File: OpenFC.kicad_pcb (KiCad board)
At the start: 8 copper layers, 29.5 x 27.6 mm, 173 parts, among them J1 5V, J13 5V, J14 5V, J15 5V, J16 5V, J17 5V, J18 5V, J19 5V, J2 5V, J20 5V, J21 5V, J22 5V, J23 5V, J24 5V, J25 5V, J26 5V, J27 5V, J28 5V, J29 5V, J3 5V, J30 5V, J31 5V, J32 5V, J33 5V, J34 5V, J35 5V, J36 5V, J37 5V, J38 5V, J39 5V, J4 5V, J40 5V, J41 5V, J42 5V, J43 5V, J44 5V, J45 5V, J46 5V, J47 5V, J48 5V, J5 5V, J53 5V, J57 5V, J59 5V, J6 5V, J7 5V, J8 5V, J9 5V, P1 SM08B-SRSS-TB(LF)(SN), Q7 DMN1150UFB-7B, U1 SM06B-SRSS-TB(LF)(SN), U10 TLV75533PDBVR, U11 RP2350A_C42411118, U12 ABM8-272-T3_C20625731, U13 W25Q32RVXHJQ TR, U14 LSM6DSV16XTR, U15 XL-1010RGBC-WS2812B, U16 XL-1010RGBC-WS2812B, U17 XL-1010RGBC-WS2812B, U18 XL-1010RGBC-WS2812B, U19 ESP8285H16, U2 W25Q128JVPIQTR, U20 SX1281IMLTRT, U21 TS2306A 240GF MSM 9_C2976675, U22 XL-1010RGBC-WS2812B, U23 XL-1010RGBC-WS2812B, U24 XL-1010RGBC-WS2812B, U25 XL-1010RGBC-WS2812B, U26 XL-1010RGBC-WS2812B, U27 XL-1010RGBC-WS2812B, U28 XL-1010RGBC-WS2812B, U29 XL-1010RGBC-WS2812B, U3 XL-1010RGBC-WS2812B, U30 BMP388, U4 XL-1010RGBC-WS2812B, U5 XL-1010RGBC-WS2812B, U6 LMR51420YDDCR, U7 LMR51420YDDCR, U8 XL-1010RGBC-WS2812B, U9 TLV75533PDBVR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

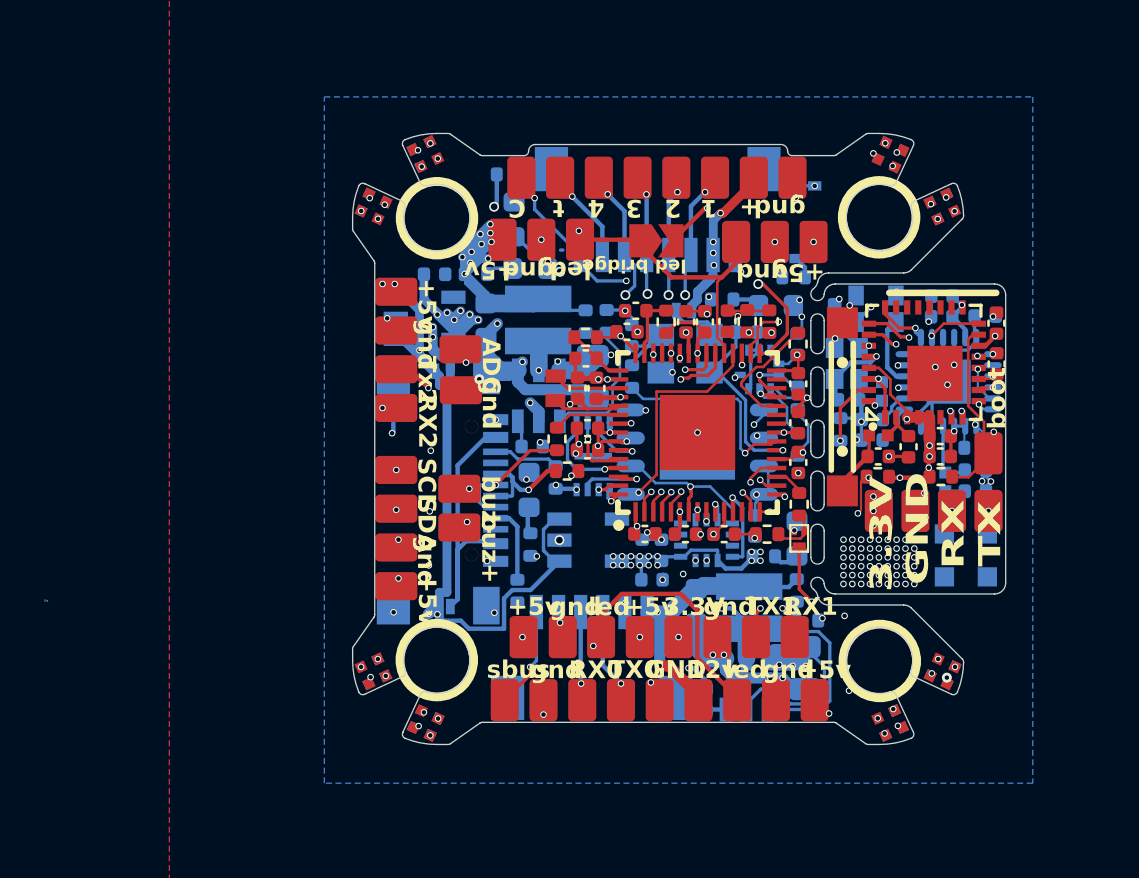
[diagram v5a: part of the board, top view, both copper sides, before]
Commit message: fixed gyro power and rp2350 inductor
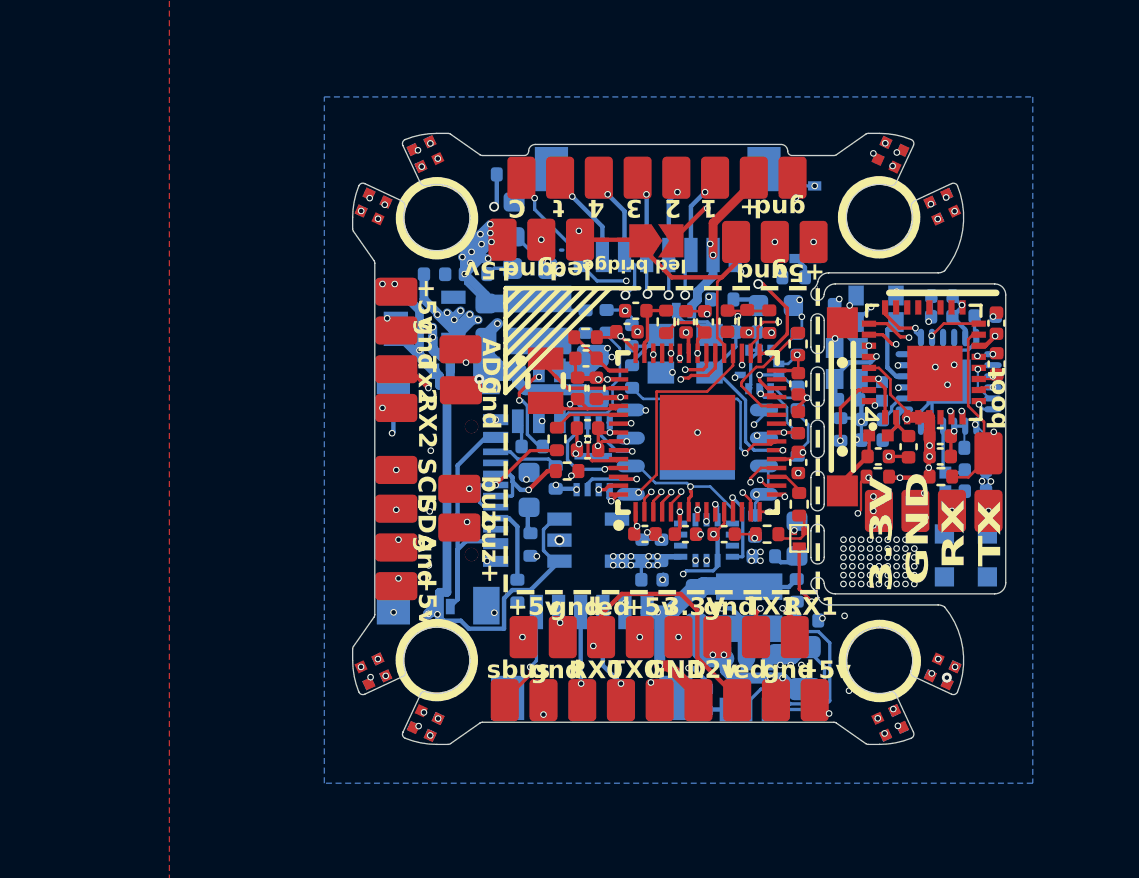
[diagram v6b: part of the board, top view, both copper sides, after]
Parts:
- removed L5: FTC160808S3R3MBCA, lib:IND-SMD_PSTMAA160808-4R7MB
- added L1: AOTA-B201610S3R3-101-T, lib:IND-SMD_L2.0-W1.6_AOTA-B201610S3R3-101-T, F.Cu at (58.0, 108.8)
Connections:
- U14 pad 5: +3.3V_GYRO -> +3.3V
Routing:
- net +BATT: track 68.9 -> 57.8 mm, vias 11 -> 9
- net +3.3V: track 77.4 -> 80.7 mm
- net +3.3V_GYRO: track 8.03 -> 10.5 mm, vias 16 -> 14
- net /LED: track 48.9 -> 49.7 mm
- net Net-(U11-VREG_LX): track 3.08 -> 3.69 mm
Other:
- outline, holes or cut-outs redrawn
- board text added: "EXPRESSLRS"
- board text added: "receiver"
- board text removed: "i2c"

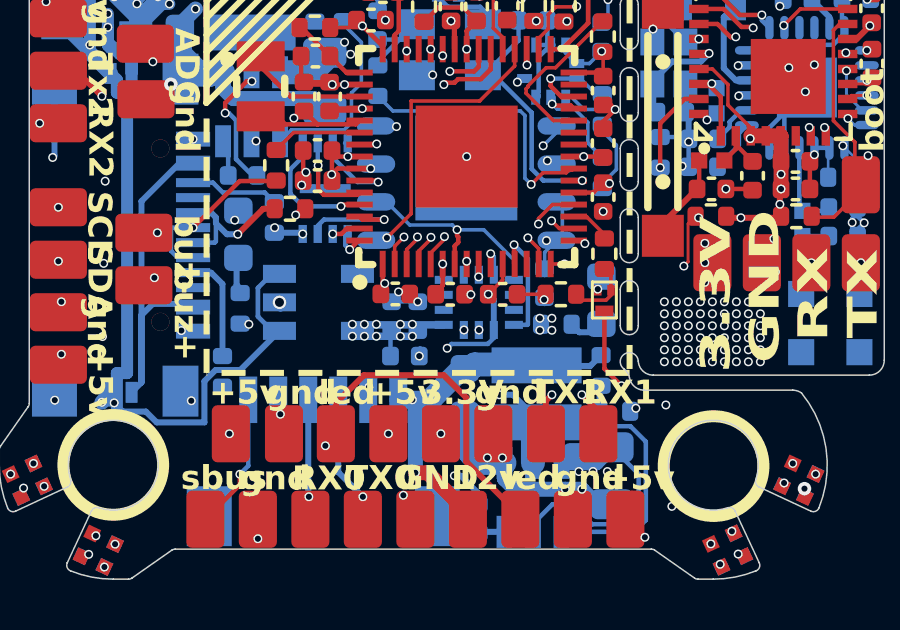
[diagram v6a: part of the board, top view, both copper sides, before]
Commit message: added silkscreen graphics
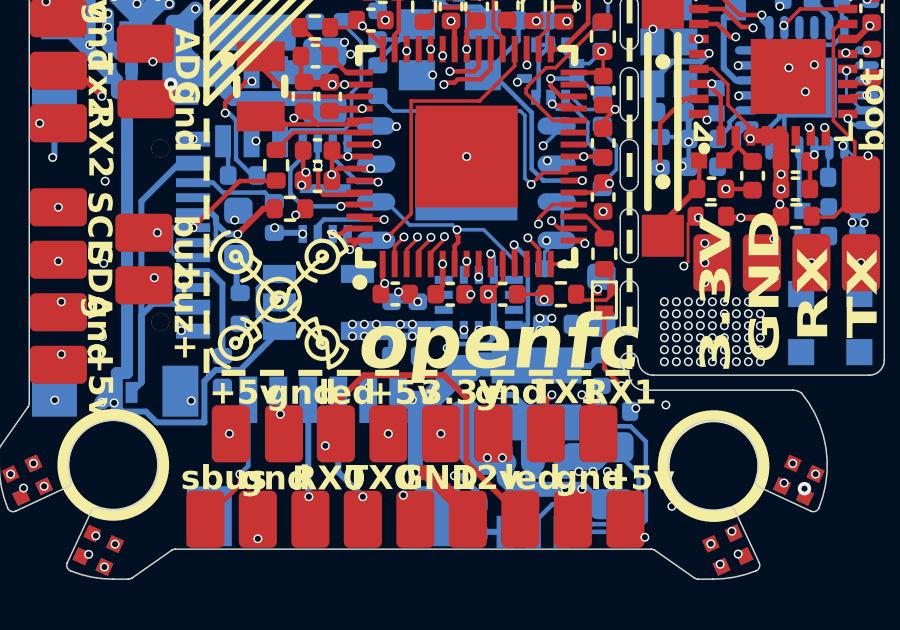
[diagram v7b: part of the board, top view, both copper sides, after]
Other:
- board text added: "openfc"
